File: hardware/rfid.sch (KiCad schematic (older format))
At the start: 10 parts

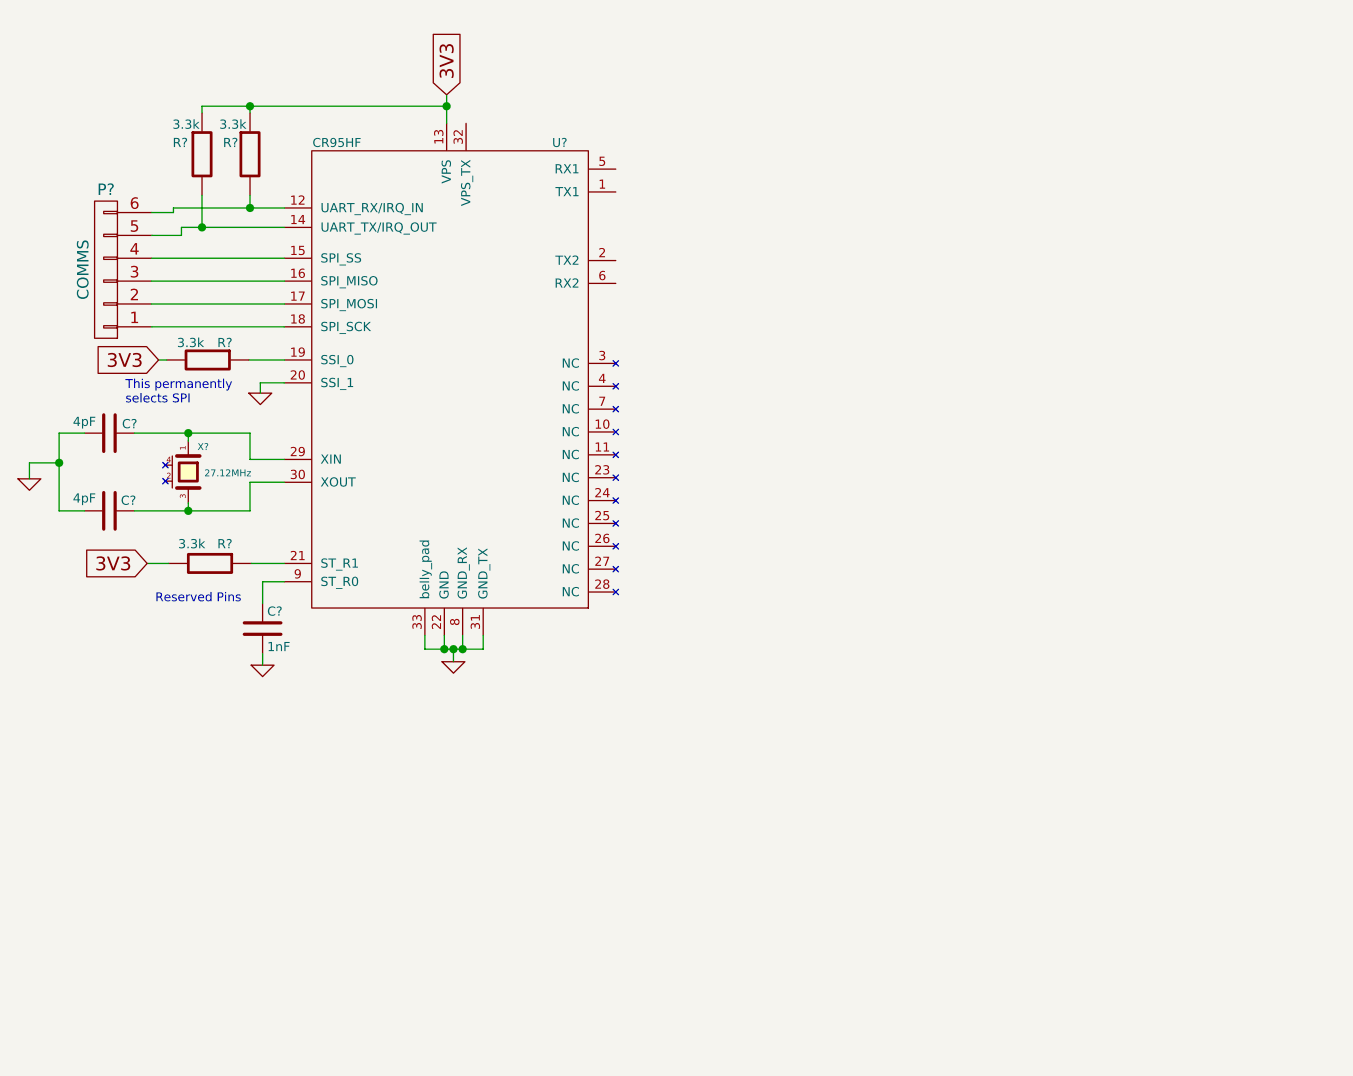
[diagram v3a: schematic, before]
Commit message: Added power connector and power conditioning passives.
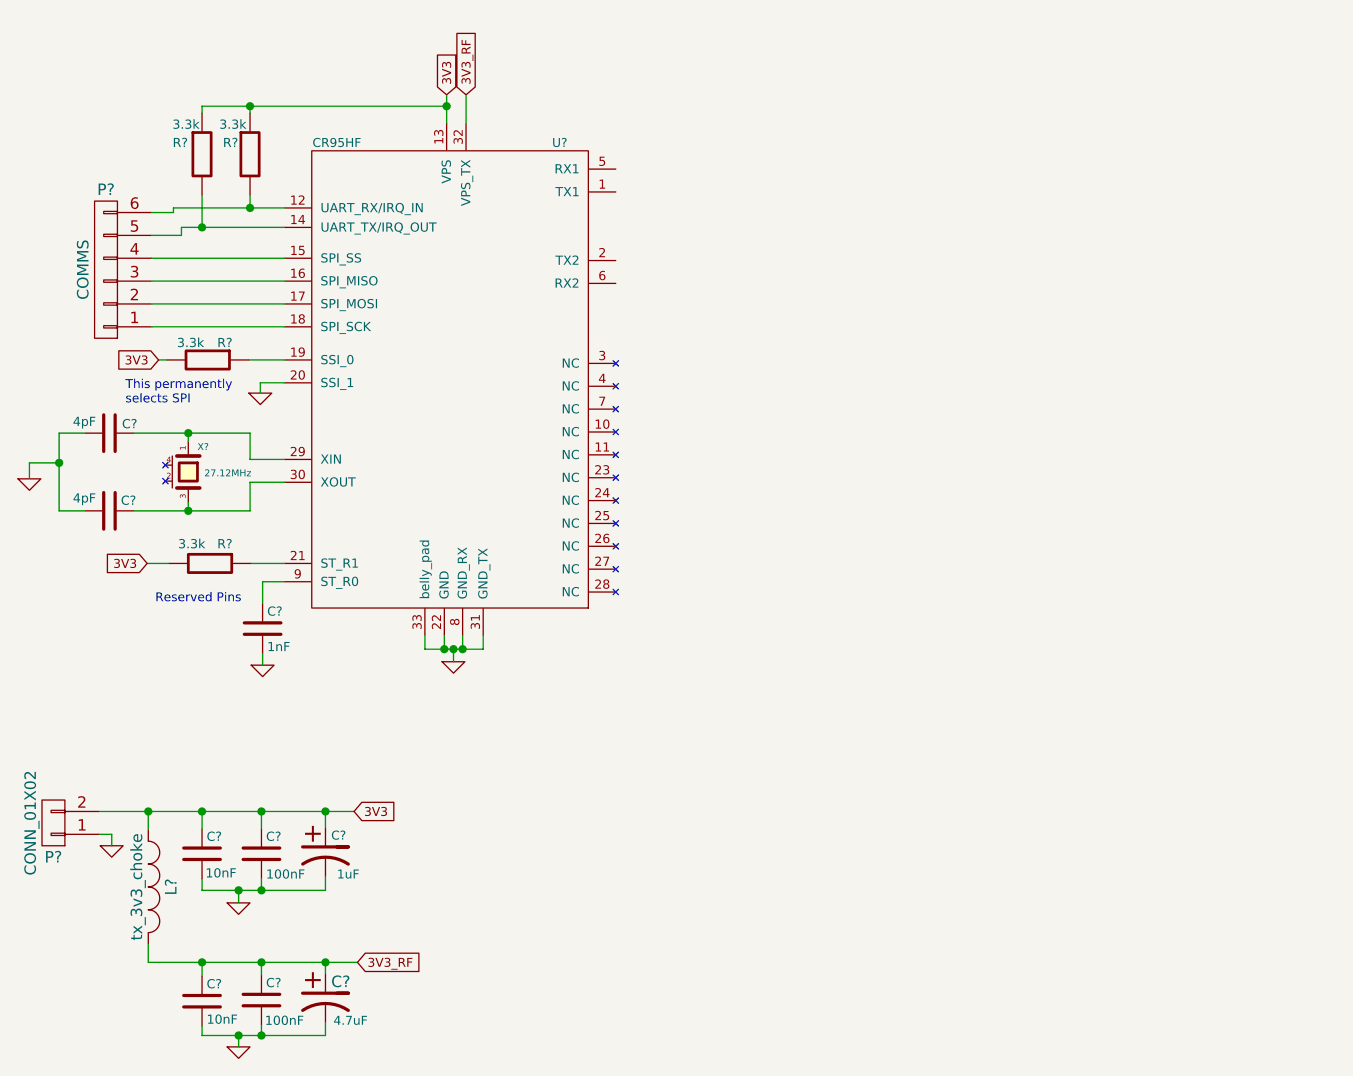
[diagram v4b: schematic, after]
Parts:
- added C? (x2): 10nF, symbol capacitor
- added C? (x2): 100nF, symbol capacitor
- added C?: 1uF, symbol Polarized_Capacitor
- added C?: 4.7uF, symbol Polarized_Capacitor
- added L?: tx_3v3_choke, symbol INDUCTOR_SMALL
- added P?: CONN_01X02, symbol CONN_01X02
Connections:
- net 3V3: now also C?.1, C?.1, C?.1, L?.1, P?.2 (P2)
- net GND: now also C?.2, C?.2, C?.2, C?.2, C?.2, C?.2, P?.1 (P1)
- net 3V3_RF: now reaches U?.32 (VPS_TX)
- net 3V3_RF: now also C?.1, C?.1, C?.1, L?.2
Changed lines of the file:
@@
 Text Notes 2220 3280 0    39   ~ 0
 Reserved Pins
-Text GLabel 3495 1050 1    60   Input ~ 0
+Text GLabel 3495 1050 1    39   Input ~ 0
 3V3
 Wire Wire Line
 	3495 1050 3495 1175
-Text GLabel 2185 3100 0    60   Input ~ 0
+Text GLabel 2185 3100 0    39   Input ~ 0
 3V3
 $Comp
@@
 	1    0    0    -1
 $EndComp
-Text GLabel 2235 2210 0    60   Input ~ 0
+Text GLabel 2235 2210 0    39   Input ~ 0
 3V3
 Wire Wire Line
@@
 	3525 3475 3525 3530
 Connection ~ 3525 3475
+$Comp
+L CONN_01X02 P?
+U 1 1 541A49C8
+P 1775 4235
+F 0 "P?" H 1775 4385 50  0000 C CNN
+F 1 "CONN_01X02" V 1875 4235 50  0000 C CNN
+F 2 "" H 1775 4235 60  0000 C CNN
+F 3 "" H 1775 4235 60  0000 C CNN
+	1    1775 4235
+	-1   0    0    1
+$EndComp
+Text GLabel 3580 1050 1    39   Input ~ 0
+3V3_RF
+Wire Wire Line
+	3580 1175 3580 1050
+$Comp
+L GND #PWR?
+U 1 1 541A5357
+P 2030 4335
+F 0 "#PWR?" H 2030 4335 30  0001 C CNN
+F 1 "GND" H 2030 4265 30  0001 C CNN
+F 2 "" H 2030 4335 60  0000 C CNN
+F 3 "" H 2030 4335 60  0000 C CNN
+	1    2030 4335
+	1    0    0    -1
+$EndComp
+Wire Wire Line
+	1975 4285 2030 4285
+Wire Wire Line
+	2030 4285 2030 4335
+Wire Wire Line
+	1975 4185 3090 4185
+Text GLabel 3090 4185 2    39   Input ~ 0
+3V3
+Text GLabel 3105 4845 2    39   Input ~ 0
+3V3_RF
+$Comp
+L INDUCTOR_SMALL L?
+U 1 1 541A56A3
+P 2190 4515
+F 0 "L?" H 2190 4615 50  0000 C CNN
+F 1 "tx_3v3_choke" H 2190 4465 50  0000 C CNN
+F 2 "" H 2190 4515 60  0000 C CNN
+F 3 "" H 2190 4515 60  0000 C CNN
+	1    2190 4515
+	0    1    1    0
+$EndComp
+$Comp
+L capacitor C?
+U 1 1 541A58CF
+P 2425 4370
+F 0 "C?" H 2445 4445 40  0000 L CNN
+F 1 "10nF" H 2440 4285 40  0000 L CNN
+F 2 "" H 2463 4220 30  0000 C CNN
+F 3 "" H 2425 4370 60  0000 C CNN
+	1    2425 4370
+	1    0    0    -1
+$EndComp
+$Comp
+L capacitor C?
+U 1 1 541A5A22
+P 2685 4370
+F 0 "C?" H 2705 4445 40  0000 L CNN
+F 1 "100nF" H 2705 4280 40  0000 L CNN
+F 2 "" H 2723 4220 30  0000 C CNN
+F 3 "" H 2685 4370 60  0000 C CNN
+	1    2685 4370
+	1    0    0    -1
+$EndComp
+$Comp
+L Polarized_Capacitor C?
+U 1 1 541A5A83
+P 2965 4365
+F 0 "C?" H 2990 4440 39  0000 L CNN
+F 1 "1uF" H 3015 4270 39  0000 L CNN
+F 2 "" H 2965 4365 60  0000 C CNN
+F 3 "" H 2965 4365 60  0000 C CNN
+	1    2965 4365
+	1    0    0    -1
+$EndComp
+$Comp
+L Polarized_Capacitor C?
+U 1 1 541A5D75
+P 2965 5005
+F 0 "C?" H 2990 5080 50  0000 L CNN
+F 1 "4.7uF" H 3000 4910 39  0000 L CNN
+F 2 "" H 2965 5005 60  0000 C CNN
+F 3 "" H 2965 5005 60  0000 C CNN
+	1    2965 5005
+	1    0    0    -1
+$EndComp
+$Comp
+L capacitor C?
+U 1 1 541A5E22
+P 2685 5010
+F 0 "C?" H 2705 5085 40  0000 L CNN
+F 1 "100nF" H 2700 4920 40  0000 L CNN
+F 2 "" H 2723 4860 30  0000 C CNN
+F 3 "" H 2685 5010 60  0000 C CNN
+	1    2685 5010
+	1    0    0    -1
+$EndComp
+$Comp
+L capacitor C?
+U 1 1 541A5EC3
+P 2425 5015
+F 0 "C?" H 2445 5090 40  0000 L CNN
+F 1 "10nF" H 2445 4935 40  0000 L CNN
+F 2 "" H 2463 4865 30  0000 C CNN
+F 3 "" H 2425 5015 60  0000 C CNN
+	1    2425 5015
+	1    0    0    -1
+$EndComp
+Wire Wire Line
+	2425 4185 2425 4260
+Connection ~ 2425 4185
+Wire Wire Line
+	2685 4260 2685 4185
+Connection ~ 2685 4185
+Wire Wire Line
+	2965 4255 2965 4185
+Connection ~ 2965 4185
+Wire Wire Line
+	2190 4265 2190 4185
+Connection ~ 2190 4185
+Wire Wire Line
+	3105 4845 2190 4845
+Wire Wire Line
+	2190 4845 2190 4765
+Wire Wire Line
+	2425 4905 2425 4845
+Connection ~ 2425 4845
+Wire Wire Line
+	2685 4900 2685 4845
+Connection ~ 2685 4845
+Wire Wire Line
+	2965 4895 2965 4845
+Connection ~ 2965 4845
+$Comp
+L GND #PWR?
+U 1 1 541A734A
+P 2585 4585
+F 0 "#PWR?" H 2585 4585 30  0001 C CNN
+F 1 "GND" H 2585 4515 30  0001 C CNN
+F 2 "" H 2585 4585 60  0000 C CNN
+F 3 "" H 2585 4585 60  0000 C CNN
+	1    2585 4585
+	1    0    0    -1
+$EndComp
+$Comp
+L GND #PWR?
+U 1 1 541A750E
+P 2585 5215
+F 0 "#PWR?" H 2585 5215 30  0001 C CNN
+F 1 "GND" H 2585 5145 30  0001 C CNN
+F 2 "" H 2585 5215 60  0000 C CNN
+F 3 "" H 2585 5215 60  0000 C CNN
+	1    2585 5215
+	1    0    0    -1
+$EndComp
+Wire Wire Line
+	2425 4480 2425 4530
+Wire Wire Line
+	2425 4530 2965 4530
+Wire Wire Line
+	2965 4530 2965 4470
+Wire Wire Line
+	2685 4480 2685 4530
+Connection ~ 2685 4530
+Wire Wire Line
+	2585 4585 2585 4530
+Connection ~ 2585 4530
+Wire Wire Line
+	2425 5125 2425 5165
+Wire Wire Line
+	2425 5165 2965 5165
+Wire Wire Line
+	2965 5165 2965 5110
+Wire Wire Line
+	2685 5120 2685 5165
+Connection ~ 2685 5165
+Wire Wire Line
+	2585 5215 2585 5165
+Connection ~ 2585 5165
 $EndSCHEMATC

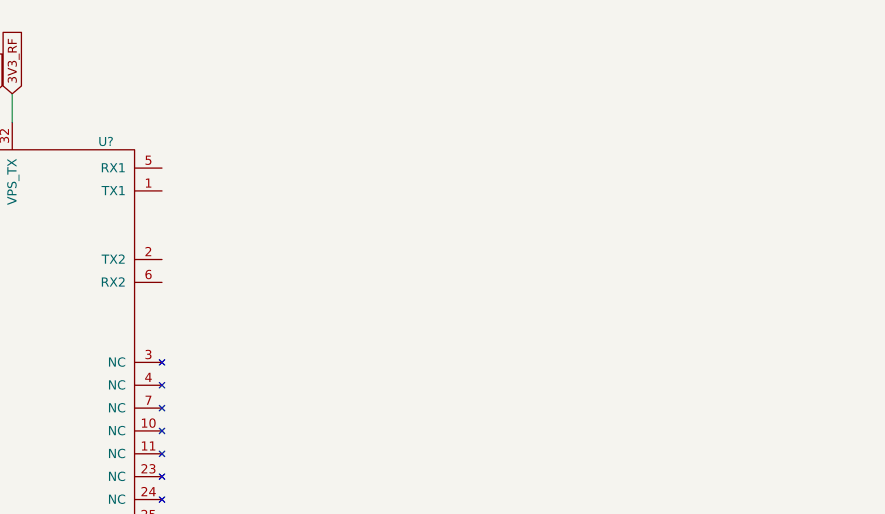
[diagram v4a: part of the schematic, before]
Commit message: Added components for antenna (straight from stmicro AN3394.
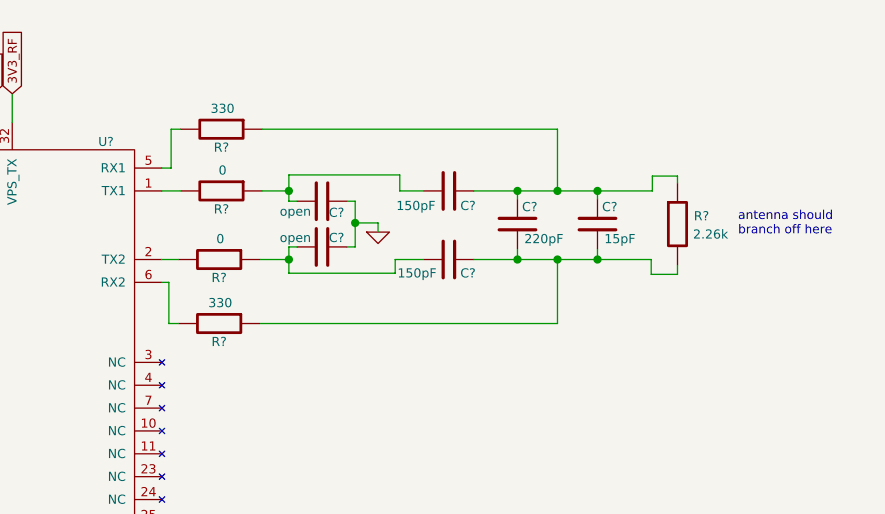
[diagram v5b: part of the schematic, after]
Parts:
- added C? (x2): open, symbol capacitor
- added C? (x2): 150pF, symbol capacitor
- added C?: 220pF, symbol capacitor
- added C?: 15pF, symbol capacitor
- added R? (x2): 330, symbol resistor
- added R? (x2): 0, symbol resistor
- added R?: 2.26k, symbol resistor
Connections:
- net GND: now also C?.1, C?.1
- net at U?.1 (TX1): now also R?.2
- net at U?.2 (TX2): now also R?.2
- net at U?.5 (RX1): now also R?.2
- net at U?.6 (RX2): now also R?.2
- new net: C?.2, C?.2, R?.1 (x2)
- new net: C?.1, C?.1, C?.1, R?.1, R?.1
- new net: C?.1, C?.2, C?.2, R?.1, R?.2
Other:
- note added: "antenna should \nbranch off here"
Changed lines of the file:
@@
 encoding utf-8
 Sheet 1 1
-Title ""
+Title "RFID TXRX"
 Date ""
-Rev ""
+Rev "1"
 Comp ""
 Comment1 ""
@@
 	2585 5215 2585 5165
 Connection ~ 2585 5165
+$Comp
+L capacitor C?
+U 1 1 541FBF59
+P 4935 1520
+F 0 "C?" V 4985 1550 40  0000 L CNN
+F 1 "open" V 4980 1335 40  0000 L CNN
+F 2 "" H 4973 1370 30  0000 C CNN
+F 3 "" H 4935 1520 60  0000 C CNN
+	1    4935 1520
+	0    1    1    0
+$EndComp
+$Comp
+L capacitor C?
+U 1 1 541FC0D8
+P 4935 1720
+F 0 "C?" V 4895 1750 40  0000 L CNN
+F 1 "open" V 4895 1535 40  0000 L CNN
+F 2 "" H 4973 1570 30  0000 C CNN
+F 3 "" H 4935 1720 60  0000 C CNN
+	1    4935 1720
+	0    1    1    0
+$EndComp
+$Comp
+L capacitor C?
+U 1 1 541FC26B
+P 5490 1475
+F 0 "C?" V 5555 1525 40  0000 L CNN
+F 1 "150pF" V 5555 1245 40  0000 L CNN
+F 2 "" H 5528 1325 30  0000 C CNN
+F 3 "" H 5490 1475 60  0000 C CNN
+	1    5490 1475
+	0    1    1    0
+$EndComp
+$Comp
+L capacitor C?
+U 1 1 541FC326
+P 5490 1775
+F 0 "C?" V 5550 1825 40  0000 L CNN
+F 1 "150pF" V 5550 1550 40  0000 L CNN
+F 2 "" H 5528 1625 30  0000 C CNN
+F 3 "" H 5490 1775 60  0000 C CNN
+	1    5490 1775
+	0    1    1    0
+$EndComp
+$Comp
+L capacitor C?
+U 1 1 541FC46F
+P 5790 1620
+F 0 "C?" H 5810 1695 40  0000 L CNN
+F 1 "220pF" H 5820 1555 40  0000 L CNN
+F 2 "" H 5828 1470 30  0000 C CNN
+F 3 "" H 5790 1620 60  0000 C CNN
+	1    5790 1620
+	1    0    0    -1
+$EndComp
+$Comp
+L capacitor C?
+U 1 1 541FC5B5
+P 6140 1620
+F 0 "C?" H 6160 1695 40  0000 L CNN
+F 1 "15pF" H 6170 1555 40  0000 L CNN
+F 2 "" H 6178 1470 30  0000 C CNN
+F 3 "" H 6140 1620 60  0000 C CNN
+	1    6140 1620
+	1    0    0    -1
+$EndComp
+$Comp
+L GND #PWR?
+U 1 1 541FD180
+P 5180 1655
+F 0 "#PWR?" H 5180 1655 30  0001 C CNN
+F 1 "GND" H 5180 1585 30  0001 C CNN
+F 2 "" H 5180 1655 60  0000 C CNN
+F 3 "" H 5180 1655 60  0000 C CNN
+	1    5180 1655
+	1    0    0    -1
+$EndComp
+$Comp
+L resistor R?
+U 1 1 541FD7DD
+P 4495 1205
+F 0 "R?" V 4575 1205 40  0000 C CNN
+F 1 "330" V 4405 1210 40  0000 C CNN
+F 2 "" V 4425 1205 30  0000 C CNN
+F 3 "" H 4495 1205 30  0000 C CNN
+	1    4495 1205
+	0    1    1    0
+$EndComp
+$Comp
+L resistor R?
+U 1 1 541FDA06
+P 4495 1475
+F 0 "R?" V 4575 1475 40  0000 C CNN
+F 1 "0" V 4405 1480 40  0000 C CNN
+F 2 "" V 4425 1475 30  0000 C CNN
+F 3 "" H 4495 1475 30  0000 C CNN
+	1    4495 1475
+	0    1    1    0
+$EndComp
+$Comp
+L resistor R?
+U 1 1 541FDC12
+P 4485 1775
+F 0 "R?" V 4565 1775 40  0000 C CNN
+F 1 "0" V 4395 1780 40  0000 C CNN
+F 2 "" V 4415 1775 30  0000 C CNN
+F 3 "" H 4485 1775 30  0000 C CNN
+	1    4485 1775
+	0    1    1    0
+$EndComp
+$Comp
+L resistor R?
+U 1 1 541FDD23
+P 4485 2055
+F 0 "R?" V 4565 2055 40  0000 C CNN
+F 1 "330" V 4395 2060 40  0000 C CNN
+F 2 "" V 4415 2055 30  0000 C CNN
+F 3 "" H 4485 2055 30  0000 C CNN
+	1    4485 2055
+	0    1    1    0
+$EndComp
+Wire Wire Line
+	4235 1475 4315 1475
+Wire Wire Line
+	4235 1775 4305 1775
+$Comp
+L resistor R?
+U 1 1 542007D4
+P 6490 1620
+F 0 "R?" H 6595 1655 40  0000 C CNN
+F 1 "2.26k" H 6635 1575 40  0000 C CNN
+F 2 "" V 6420 1620 30  0000 C CNN
+F 3 "" H 6490 1620 30  0000 C CNN
+	1    6490 1620
+	1    0    0    -1
+$EndComp
+Wire Wire Line
+	4235 1375 4275 1375
+Wire Wire Line
+	4275 1375 4275 1205
+Wire Wire Line
+	4275 1205 4315 1205
+Wire Wire Line
+	4235 1875 4265 1875
+Wire Wire Line
+	4265 1875 4265 2055
+Wire Wire Line
+	4265 2055 4305 2055
+Wire Wire Line
+	4675 1475 4790 1475
+Wire Wire Line
+	4790 1405 4790 1520
+Wire Wire Line
+	4790 1520 4825 1520
+Wire Wire Line
+	4665 1775 4790 1775
+Wire Wire Line
+	4790 1720 4790 1835
+Wire Wire Line
+	4790 1720 4825 1720
+Wire Wire Line
+	5045 1520 5080 1520
+Wire Wire Line
+	5080 1520 5080 1720
+Wire Wire Line
+	5080 1720 5045 1720
+Wire Wire Line
+	5080 1615 5180 1615
+Wire Wire Line
+	5180 1615 5180 1655
+Connection ~ 5080 1615
+Wire Wire Line
+	4790 1405 5275 1405
+Wire Wire Line
+	5275 1405 5275 1475
+Wire Wire Line
+	5275 1475 5380 1475
+Connection ~ 4790 1475
+Wire Wire Line
+	4790 1835 5255 1835
+Wire Wire Line
+	5255 1835 5255 1775
+Wire Wire Line
+	5255 1775 5380 1775
+Connection ~ 4790 1775
+Wire Wire Line
+	5600 1475 6380 1475
+Wire Wire Line
+	6380 1475 6380 1410
+Wire Wire Line
+	6380 1410 6490 1410
+Wire Wire Line
+	6490 1410 6490 1440
+Wire Wire Line
+	5600 1775 6375 1775
+Wire Wire Line
+	6375 1775 6375 1840
+Wire Wire Line
+	6375 1840 6490 1840
+Wire Wire Line
+	6490 1840 6490 1800
+Wire Wire Line
+	5790 1730 5790 1775
+Connection ~ 5790 1775
+Wire Wire Line
+	5790 1510 5790 1475
+Connection ~ 5790 1475
+Wire Wire Line
+	6140 1510 6140 1475
+Connection ~ 6140 1475
+Wire Wire Line
+	6140 1730 6140 1775
+Connection ~ 6140 1775
+Wire Wire Line
+	4665 2055 5965 2055
+Wire Wire Line
+	5965 2055 5965 1775
+Connection ~ 5965 1775
+Wire Wire Line
+	4675 1205 5965 1205
+Wire Wire Line
+	5965 1205 5965 1475
+Connection ~ 5965 1475
+Text Notes 6755 1675 0    39   ~ 0
+antenna should \nbranch off here
 $EndSCHEMATC
